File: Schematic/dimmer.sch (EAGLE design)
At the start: 19 parts, among them T1 SPP20N6055-N, T3 BC547, X1 W237-102°45_00

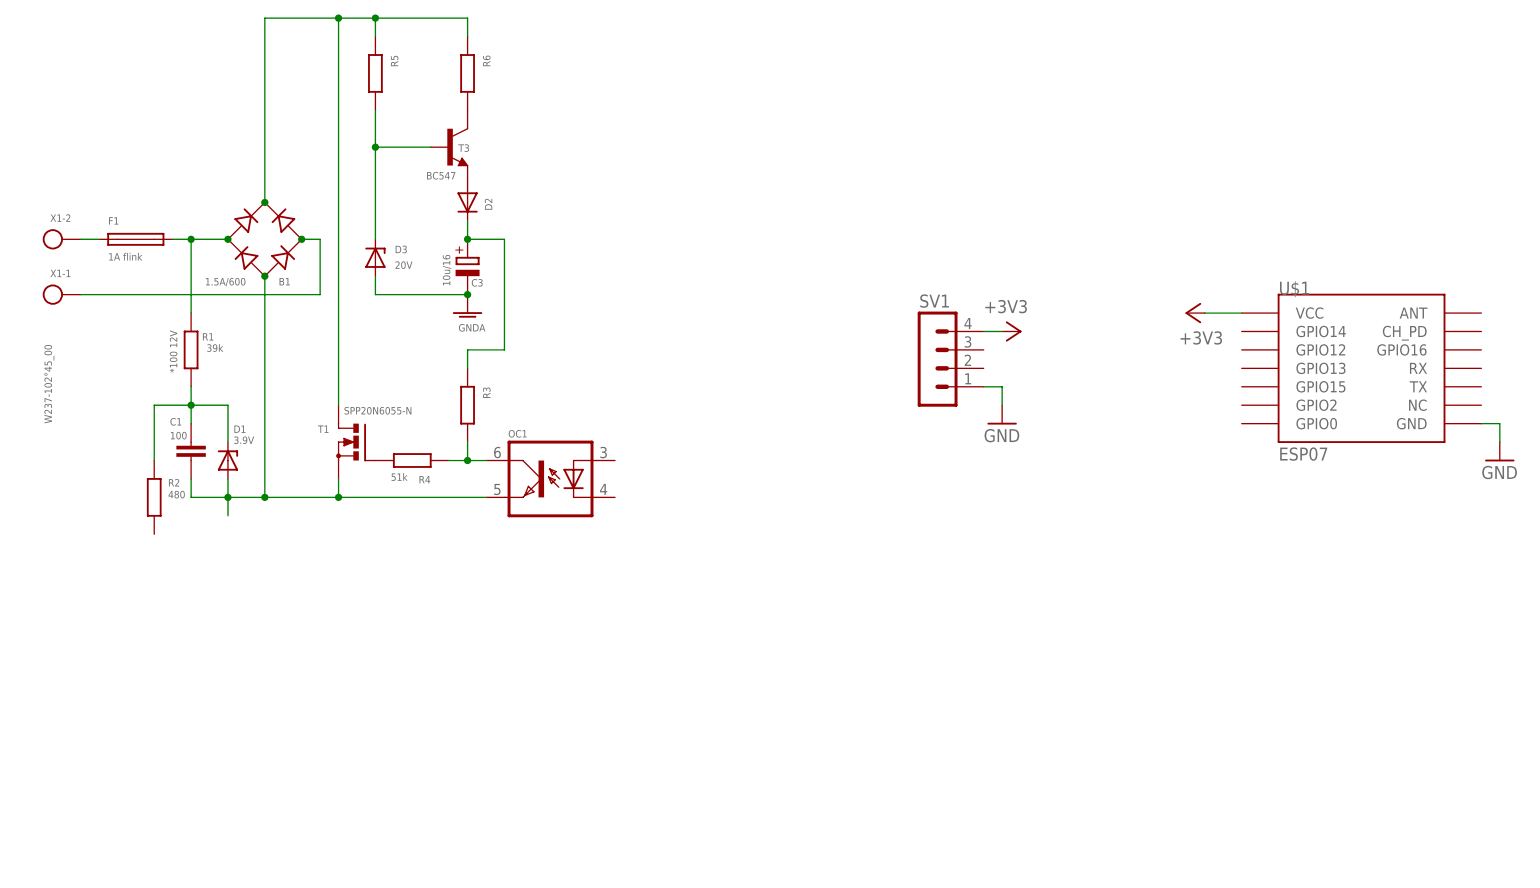
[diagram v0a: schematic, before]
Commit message: Driectly drive MOSFET (No mathing MOSFET found)
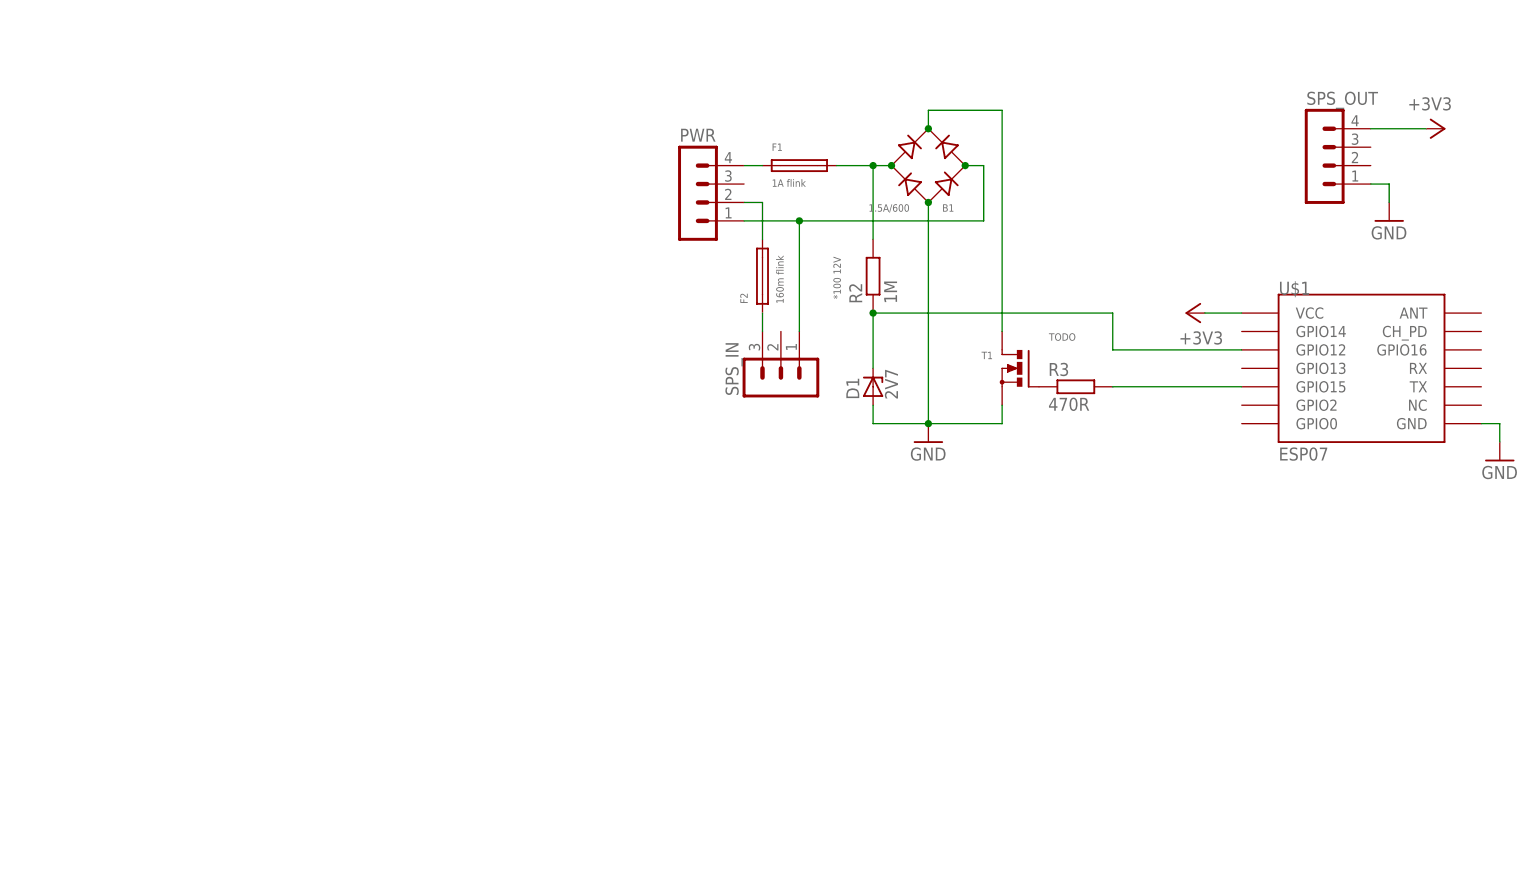
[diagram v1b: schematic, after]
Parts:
- removed C1: 100, rcl:C-EU050-025X075
- removed C3: 10u/16, rcl:CPOL-EUE2.5-6
- removed D2: (no value), diode:DIODE-D-7.5
- removed D3: 20V, diode:BZX90N
- removed R1: 39k, rcl:R-EU_0204/12
- removed R4: 51k, rcl:R-EU_M1206
- removed R5, R6: (no value), rcl:R-EU_M1206
- removed SV1: (no value), con-lstb:MA04-1
- removed T3: BC547, transistor-npn:BC547
- removed U$3: OC1, optocoupler:ILD205SOCI08-N
- removed X1: W237-102°45_00, con-wago-500:W237-102°45_00
- added F2: 160m flink, fuse:19560
- added PWR, SPS_OUT: (no value), con-lstb:MA04-1
- added SPS_IN: (no value), con-lstb:MA03-1
- D1: value 3.9V -> 2V7; device diode:BZX90SMD -> diode:ZENER-DIODEF126-12
- R2: value 480 -> 1M; device rcl:R-EU_M1206 -> rcl:R-EU_0207/12
- R3: value (none) -> 470R; device rcl:R-EU_M1206 -> rcl:R-EU_0207/12
- T1: value SPP20N6055-N -> TODO
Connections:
- removed net GNDA: B1.-, C1.2, C3.-, D1.A, D3.A, T1.S, U$3G$2.EMIT
- removed net N$6: D2.A, T3.E
- removed net N$7: C3.+, D2.C, R3.1
- net +3V3: now also SPS_OUT.4; no longer SV1.4
- net GND: now also B1.-, D1.A, SPS_OUT.1, T1.S; no longer SV1.1
- net N$1: now also R3.1; no longer R4.2
- net N$17: now also R2.2; no longer R1.1
- net N$2: now also U$1.GPIO15; no longer R4.1, U$3G$2.COL
- net N$21: no longer R5.1, R6.1
- net N$3: now also PWR.1, SPS_IN.1; no longer X1-1.KL
- net N$30: now also R2.1, U$1.GPIO12; no longer C1.1, R1.2, R2.2
- net N$31: now also PWR.4; no longer X1-2.KL
- net N$4: now also F2.2, PWR.2; no longer R6.2, T3.C
- net N$5: now also F2.1, SPS_IN.3; no longer D3.C, R5.2, T3.B
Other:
- moved on the sheet: B1, F1, R2, R3, T1

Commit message: Use own package for SMPS
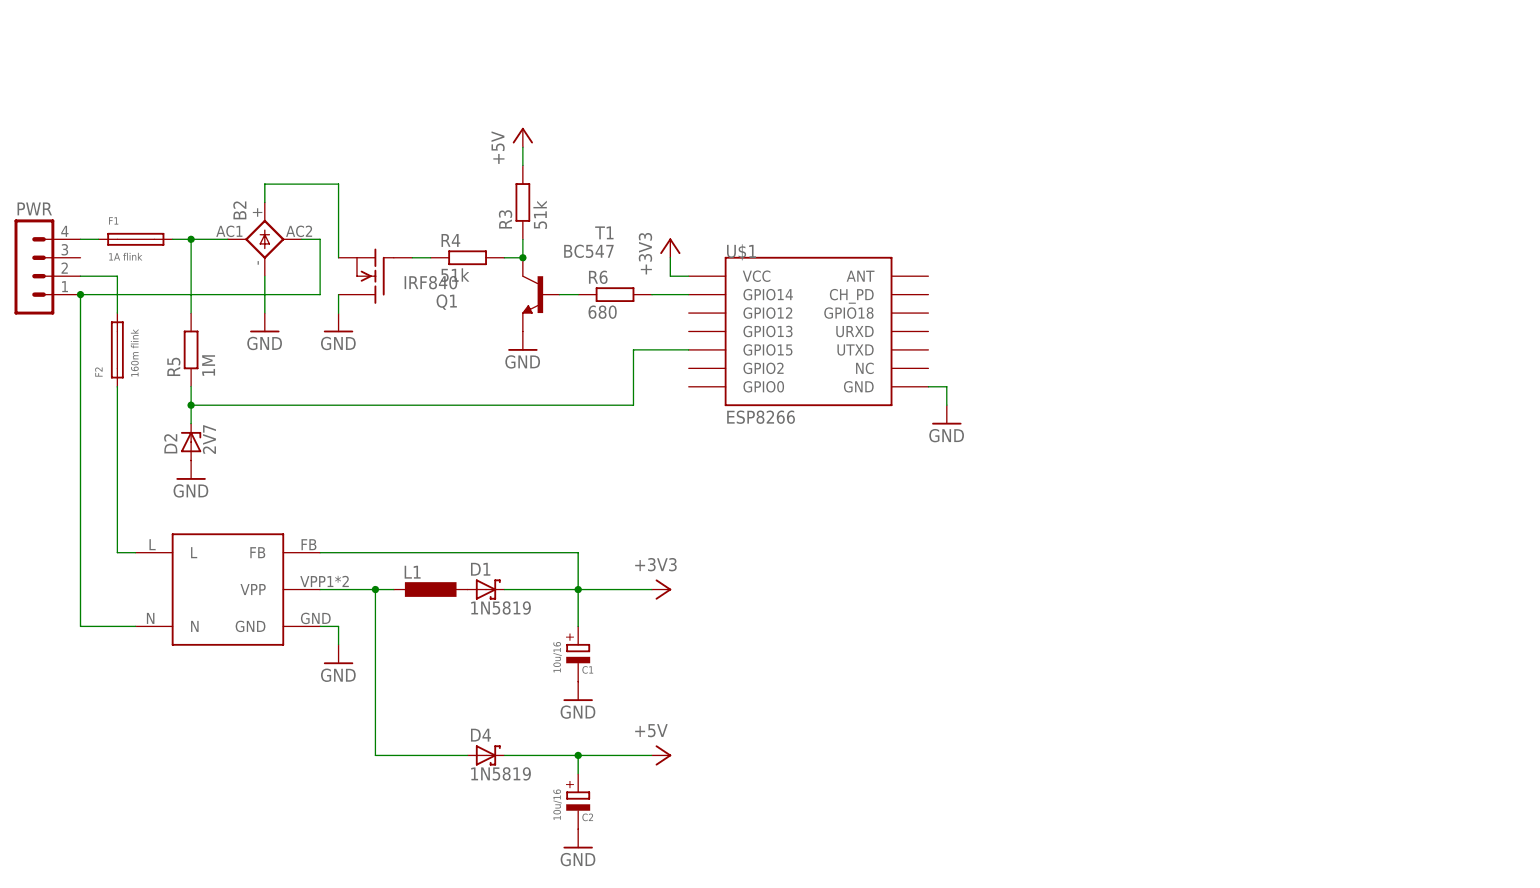
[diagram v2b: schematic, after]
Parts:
- removed B1: 1.5A/600, rectifier:RB1A
- removed R2: 1M, rcl:R-EU_0207/12
- removed SPS_IN: (no value), con-lstb:MA03-1
- removed SPS_OUT: (no value), con-lstb:MA04-1
- added B2: (no value), rectifier:2KBP
- added C1, C2: 10u/16, rcl:CPOL-EUE2.5-6
- added D2: 2V7, diode:ZENER-DIODEF126-12
- added D4: 1N5819, diode:1N5908
- added L1: (no value), rcl:L-EU0204/5
- added Q1: IRF840, transistor-fet:IRF840
- added R4: 51k, rcl:R-EU_0207/12
- added R5: 1M, rcl:R-EU_0207/12
- added R6: 680, rcl:R-EU_0207/10
- added U$2: SMPS, smps:SMPS
- D1: value 2V7 -> 1N5819; device diode:ZENER-DIODEF126-12 -> diode:1N5908
- R3: value 470R -> 51k; device rcl:R-EU_0207/12 -> rcl:R-EU_0207/10
- T1: value TODO -> BC547; device transistor-power:SPP20N6055-N -> transistor:BC547
- U$1: value ESP07 -> ESP8266; device esp8266modules:ESP07 -> esp8266modules:ESP8266
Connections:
- removed net N$30: D1.C, R2.1, U$1.GPIO12
- new net +5V: C2.+, D4.C, R3.2
- new net N$12: R6.2, U$1.GPIO14
- new net N$4: B2.AC2, PWR.1, U$2.N
- new net N$6: D4.A, L1.2, U$2.VPP
- new net N$7: D2.C, R5.1, U$1.GPIO15
- new net N$9: F2.1, U$2.L
- net +3V3: now also C1.+, D1.C, U$2.FB; no longer SPS_OUT.4
- net GND: now also B2.-, C1.-, C2.-, D2.A, Q1.D, T1.E, U$2.GND; no longer B1.-, D1.A, SPS_OUT.1, T1.S
- net N$1: now also Q1.G, R4.1; no longer R3.1, T1.G
- net N$17: now also B2.AC1, R5.2; no longer B1.AC1, R2.2
- net N$2: now also R3.1, R4.2, T1.C; no longer R3.2, U$1.GPIO15
- net N$21: now also B2.+, Q1.S; no longer B1.+, T1.D
- net N$3: now also D1.A, L1.1; no longer B1.AC2, PWR.1, SPS_IN.1
- net N$5: now also R6.1, T1.B; no longer F2.1, SPS_IN.3
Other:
- note removed: "*100 12V"
- moved on the sheet: F1, F2, PWR, R3, U$1

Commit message: Add tasters
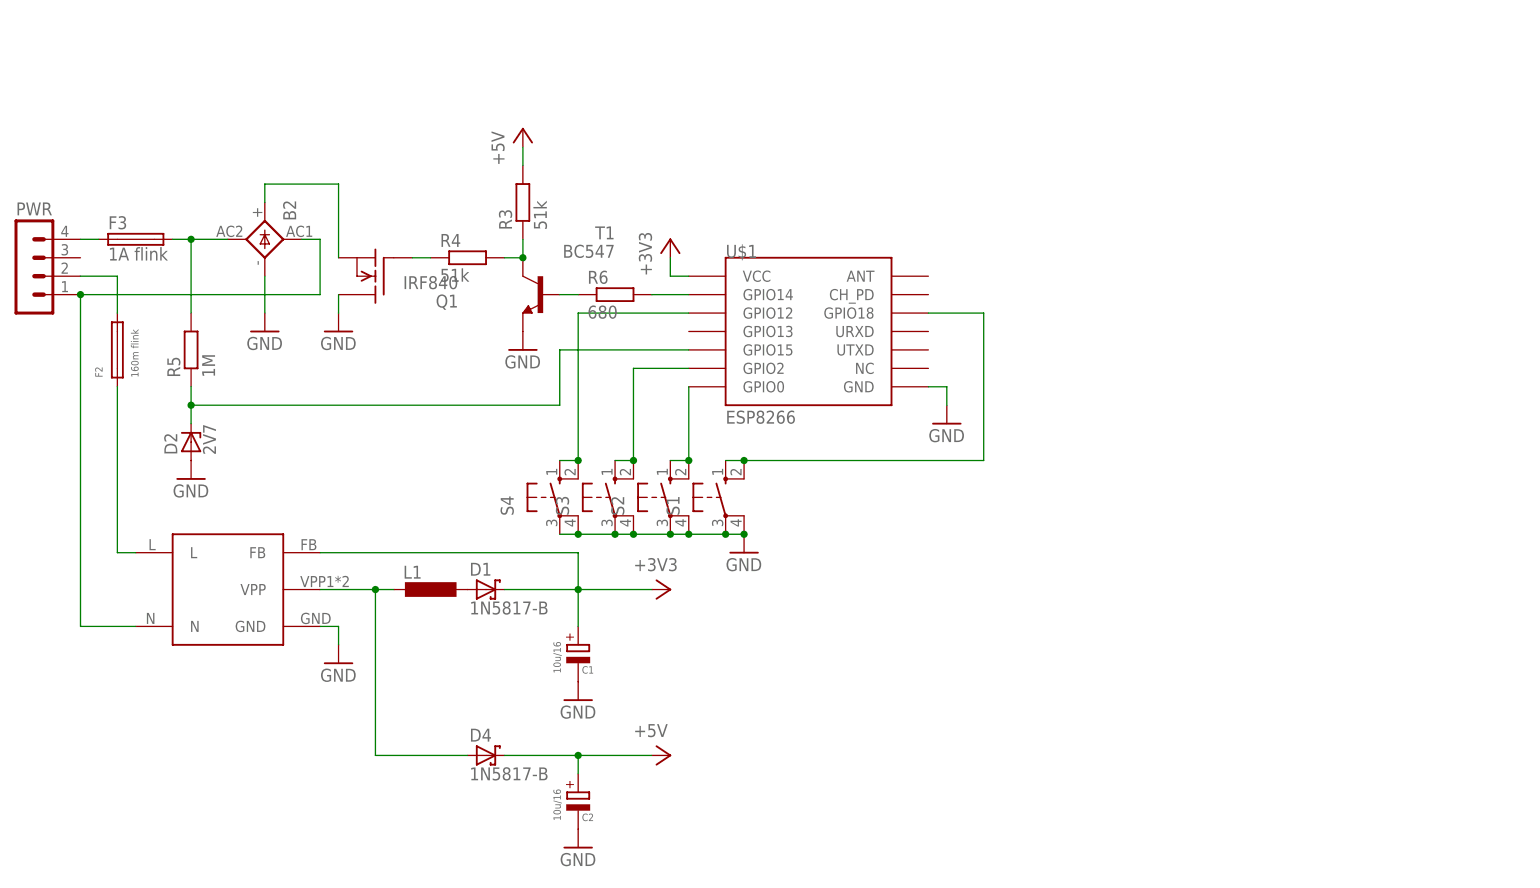
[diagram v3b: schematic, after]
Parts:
- removed F1: 1A flink, fuse:19560
- added F3: 1A flink, fuse:FUSESHK20L
- added S1, S2, S3, S4: (no value), switch-omron:10-XX
- D1, D4: value 1N5819 -> 1N5817-B; device diode:1N5908 -> diode:1N5817-B
- D2: device diode:ZENER-DIODEF126-12 -> diode:ZENER-DIODEDO34-7
- R3: device rcl:R-EU_0207/10 -> rcl:R-EU_0204/5
- R4: device rcl:R-EU_0207/12 -> rcl:R-EU_0207/10
- R6: device rcl:R-EU_0207/10 -> rcl:R-EU_0204/7
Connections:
- new net N$13: S2.S, S2.S1, U$1.GPIO0
- new net N$14: S3.S, S3.S1, U$1.GPIO2
- new net N$15: S1.S, S1.S1, U$1.GPIO18
- new net N$16: S4.S, S4.S1, U$1.GPIO12
- net GND: now also S1.P, S1.P1, S2.P, S2.P1, S3.P, S3.P1, S4.P, S4.P1
- net N$17: now also B2.AC2, F3.2; no longer B2.AC1, F1.2
- net N$31: now also F3.1; no longer F1.1
- net N$4: now also B2.AC1; no longer B2.AC2
